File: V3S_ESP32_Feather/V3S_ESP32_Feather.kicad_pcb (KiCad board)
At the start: 4 copper layers, 22.9 x 50.8 mm, 76 parts, among them J1 USB_C_Receptacle_USB2.0, J2 Bat, J4 PWM, J5 U.FL-R-SMT(01), J6 UART, J7 Micro_SD_Card_Det, J8 I2C, J9 SPI, Q1 S8050(SOT-23), U1 V3S, U2 FUSB302B01MPX, U4 ICM-20948, U5 ESP32-PICO-D4, U6 MCP73831T-4ADI_OT, U7 BMP280, U8 INA219AIDCNR, Y1 X1E0000210832, Y2 CC5V-T1A 32.768KHZ +-20PPM 12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

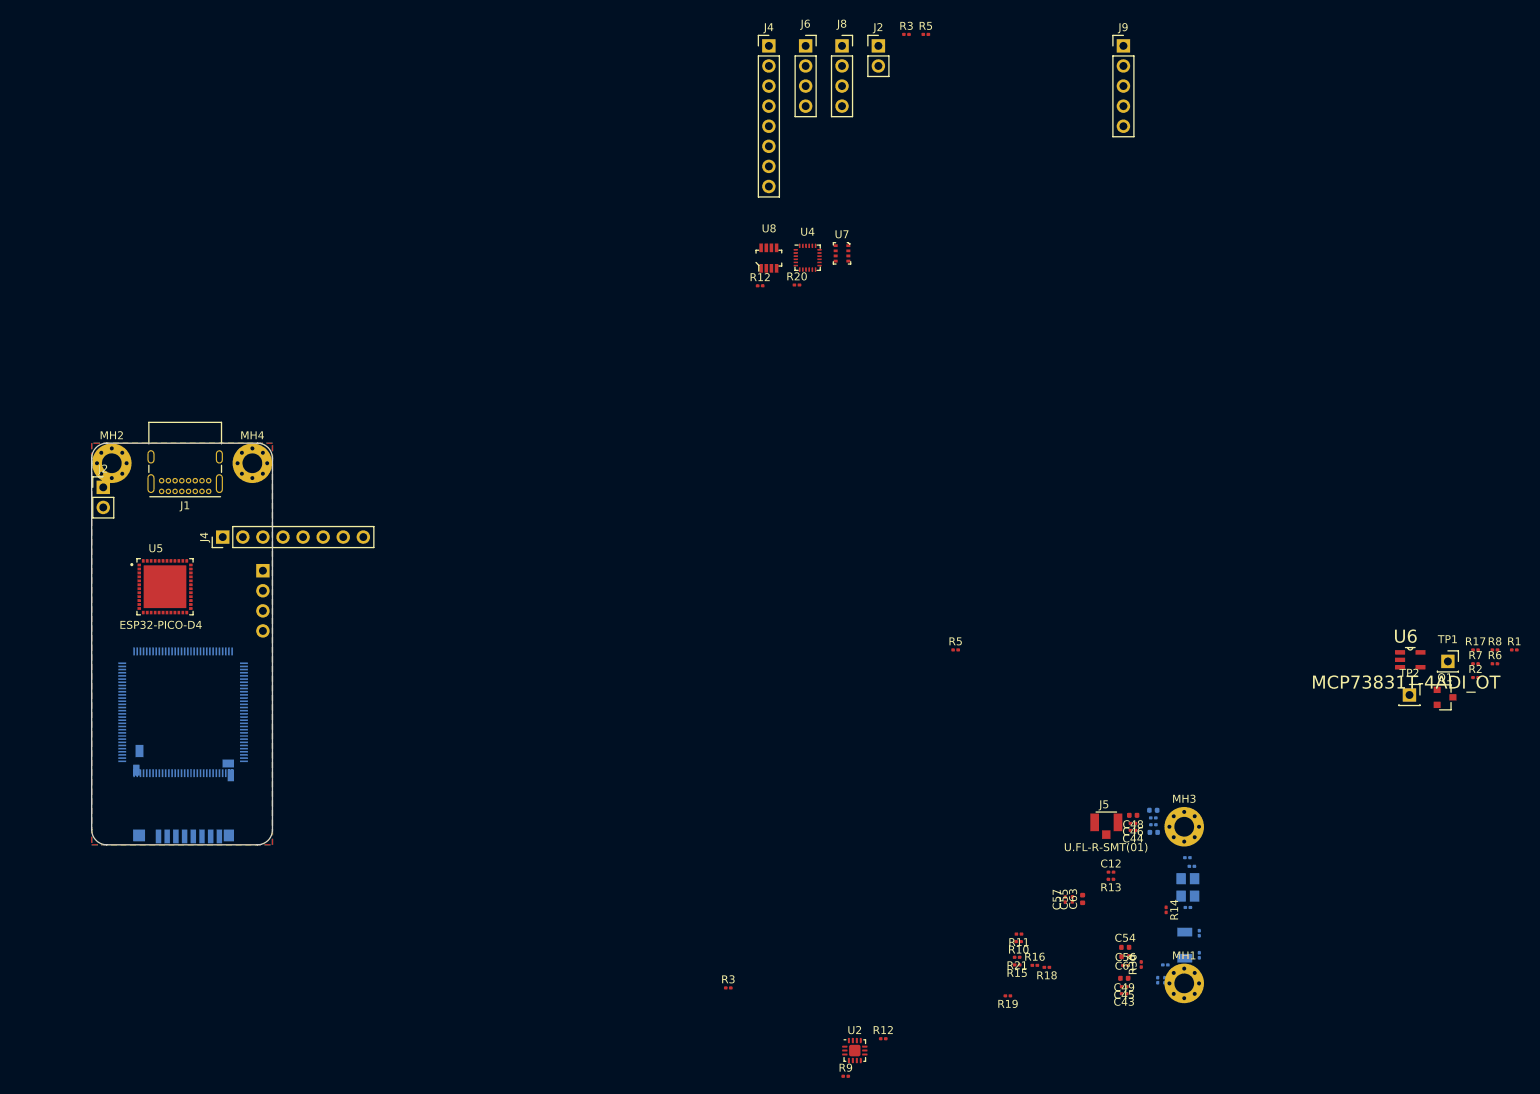
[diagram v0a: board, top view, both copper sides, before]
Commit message: Add more footprint, pcb format done, started component placement
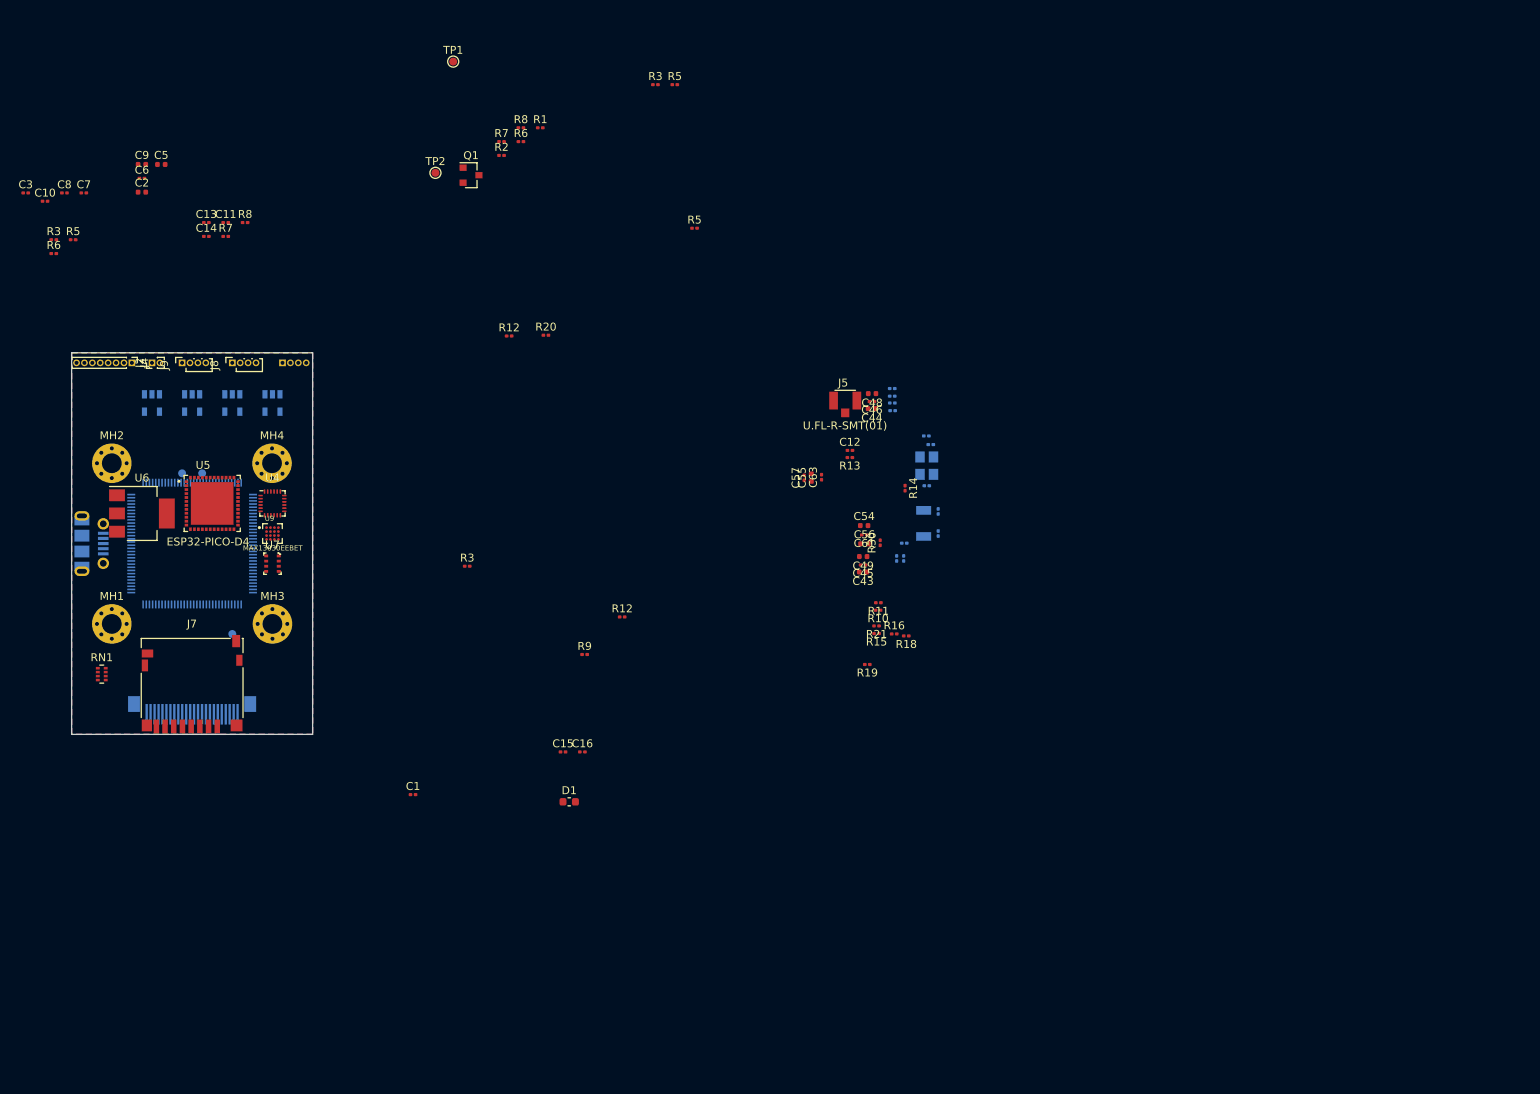
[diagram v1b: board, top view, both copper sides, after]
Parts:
- removed the J2 at (124.9, -18.5)
- removed the J4 at (111.0, -18.5)
- removed the J6 at (115.7, -18.5)
- removed R17: 470R, Resistor_SMD:R_0201_0603Metric
- added C1: 100nF, Capacitor_SMD:C_0201_0603Metric, F.Cu at (66.0, 76.2)
- added C10: 1uF, Capacitor_SMD:C_0201_0603Metric, F.Cu at (19.5, 1.15)
- added C11: 0.1uF, Capacitor_SMD:C_0201_0603Metric, F.Cu at (42.4, 3.85)
- added C13: 1uF, Capacitor_SMD:C_0201_0603Metric, F.Cu at (39.9, 3.85)
- added C14: 0.1uF, Capacitor_SMD:C_0201_0603Metric, F.Cu at (39.9, 5.60)
- added C15: 100nF, Capacitor_SMD:C_0201_0603Metric, F.Cu at (85.0, 70.8)
- added C16: 100nF, Capacitor_SMD:C_0201_0603Metric, F.Cu at (87.5, 70.8)
- added C2: 10uF, Capacitor_SMD:C_0402_1005Metric, F.Cu at (31.8, 0.00)
- added C3: 1uF, Capacitor_SMD:C_0201_0603Metric, F.Cu at (17.1, 0.10)
- added C5: 10uF, Capacitor_SMD:C_0402_1005Metric, F.Cu at (34.2, -3.50)
- added C6: 1uF, Capacitor_SMD:C_0201_0603Metric, F.Cu at (31.8, -1.75)
- added C7: 4.7uF, Capacitor_SMD:C_0201_0603Metric, F.Cu at (24.4, 0.10)
- added C8: 4.7uF, Capacitor_SMD:C_0201_0603Metric, F.Cu at (21.9, 0.10)
- added C9: 10uF, Capacitor_SMD:C_0402_1005Metric, F.Cu at (31.8, -3.50)
- added D1: D, Resistor_SMD:R_0603_1608Metric, F.Cu at (85.8, 77.1)
- added J3: CAM, fpc_cam24:FPC_24_CAM, B.Cu at (38.1, 66.0)
- added R3: 47K, Resistor_SMD:R_0201_0603Metric, F.Cu at (20.6, 6.02)
- added R5: 10K, Resistor_SMD:R_0201_0603Metric, F.Cu at (23.1, 6.02)
- added R6: 10K, Resistor_SMD:R_0201_0603Metric, F.Cu at (20.6, 7.77)
- added R7: R, Resistor_SMD:R_0201_0603Metric, F.Cu at (42.4, 5.60)
- added R8: R, Resistor_SMD:R_0201_0603Metric, F.Cu at (44.8, 3.85)
- added RN1: 47K, Resistor_SMD:R_Array_Concave_4x0402, F.Cu at (26.7, 61.0)
- added TP2: CPU_RX, TestPoint:TestPoint_Pad_D1.0mm, B.Cu at (36.8, 35.6)
- added TP3: CPU_TX, TestPoint:TestPoint_Pad_D1.0mm, B.Cu at (39.4, 35.6)
- added TP4: CPU_RST, TestPoint:TestPoint_Pad_D1.0mm, B.Cu at (43.2, 55.9)
- added U2: MIC5504-1.2YM5, Package_TO_SOT_SMD:SOT-23-5, B.Cu at (43.2, 26.7)
- added U3: MIC5501-3.0YM5, Package_TO_SOT_SMD:SOT-23-5, B.Cu at (33.0, 26.7)
- added U9: MAX13030EEBET, MAX13030EEBET:BGA16C50P4X4_202X202X67N, F.Cu at (48.3, 43.2)
- C43, C44, C55, C56: footprint Capacitor_SMD:C_0201_0603Metric -> Capacitor_SMD:C_0402_1005Metric
- C61, C63, C64, C65: footprint Capacitor_SMD:C_0402_1005Metric -> Capacitor_SMD:C_0201_0603Metric
- J1: value USB_C_Receptacle_USB2.0 -> USB_B_Micro; footprint Connector_USB:USB_C_Receptacle_GCT_USB4085 -> Connector_USB:USB_Micro-B_Molex-105017-0001; moved to B.Cu
- J2: footprint Connector_PinHeader_2.54mm:PinHeader_1x02_P2.54mm_Vertical -> Connector_PinHeader_1.00mm:PinHeader_1x02_P1.00mm_Vertical
- J4: footprint Connector_PinHeader_2.54mm:PinHeader_1x08_P2.54mm_Vertical -> Connector_PinHeader_1.00mm:PinHeader_1x08_P1.00mm_Vertical
- J6: footprint Connector_PinSocket_2.54mm:PinSocket_1x04_P2.54mm_Vertical -> Connector_PinHeader_1.00mm:PinHeader_1x04_P1.00mm_Vertical
- J7: moved to F.Cu
- J8: footprint Connector_PinSocket_2.54mm:PinSocket_1x04_P2.54mm_Vertical -> Connector_PinSocket_1.00mm:PinSocket_1x04_P1.00mm_Vertical
- J9: value SPI -> I2C; footprint Connector_PinHeader_2.54mm:PinHeader_1x05_P2.54mm_Vertical -> Connector_PinSocket_1.00mm:PinSocket_1x04_P1.00mm_Vertical
- R3 (x2): value 5.1K -> 47K
- R5 (x2): value 5.1K -> 10K
- R6: value 100K -> 10K
- R7: value 0 -> R
- R8: value 2K -> R
- TP1: footprint Connector_PinSocket_2.54mm:PinSocket_1x01_P2.54mm_Vertical -> TestPoint:TestPoint_Pad_D1.0mm
- TP2: value CHRG_IN -> CPU_RX; footprint Connector_PinSocket_2.54mm:PinSocket_1x01_P2.54mm_Vertical -> TestPoint:TestPoint_Pad_D1.0mm
- U2: value FUSB302B01MPX -> MIC5504-1.2YM5; footprint Package_DFN_QFN:WQFN-14-1EP_2.5x2.5mm_P0.5mm_EP1.45x1.45mm -> Package_TO_SOT_SMD:SOT-23-5; moved to B.Cu
- U6: value MCP73831T-4ADI_OT -> LT1963AxST-3.3; footprint MCP73831T-4ADI_OT:SOT95P280X145-5N -> Package_TO_SOT_SMD:SOT-223-3_TabPin2
- U8: value INA219AIDCNR -> MIC5504-1.8YM5; footprint digikey-footprints:SOT-23-8 -> Package_TO_SOT_SMD:SOT-23-5; moved to B.Cu
- moved U6 161.5 mm to (31.8, 40.6)
- moved TP1 146.9 mm to (71.1, -16.5)
- moved MH1 143.1 mm to (27.9, 54.6)
- moved R1 139.8 mm to (82.1, -8.14)
- moved Q1 139.8 mm to (73.4, -2.14)
- moved R2 139.8 mm to (77.2, -4.64)
- moved R6 139.8 mm to (79.7, -6.39)
- moved R7 139.8 mm to (77.2, -6.39)
- moved R8 139.8 mm to (79.7, -8.14)
- moved TP2 139.8 mm to (68.9, -2.44)
- moved J9 125.6 mm to (36.8, 21.6), turned to 90 degrees
- moved MH3 118.1 mm to (48.3, 54.6)
- moved U2 110.1 mm to (48.3, 26.7), turned to 270 degrees
- moved J8 86.9 mm to (43.2, 21.6), turned to 90 degrees
- moved U7 82.0 mm to (48.3, 47.0)
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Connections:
- C44 pad 1: +3.3VA -> +3V3
- C46 pad 1: +3.3VA -> +3V3
- C48 pad 1: +3.3VA -> +3V3
- C54 pad 1: +3.3VA -> +3V3
- C56 pad 1: +3.3VA -> +3V3
- C61 pad 2: +3.3VA -> +3V3
- J6 pad 3: /TX -> (no net)
- J7 pad 10: Net-(J7-Pad10) -> (no net)
- J7 pad 9: Net-(J7-Pad9) -> (no net)
- J9 pad 2: /All V3s input output/SPI_MISO -> Net-(J9-Pad2)
- J9 pad 3: /All V3s input output/SPI_CLK -> Net-(J9-Pad3)
- J9 pad 4: /All V3s input output/SPI_MOSI -> +3V3
- Q1 pad 2: Net-(C2-Pad1) -> /PMIC Power Battery/VIN
- R3 pad 1: GND -> +3V3 (x2)
- R3 pad 2: Net-(J1-PadA5) -> /USB_ID (x2)
- R5 pad 1: GND -> +3V3 (x2)
- R5 pad 2: Net-(J1-PadB5) -> Net-(J9-Pad2) (x2)
- R6 pad 1: /PMIC Power Battery/3.3V_EN -> Net-(J9-Pad3)
- R6 pad 2: Net-(C2-Pad1) -> +3V3
- R7 pad 1: Net-(R7-Pad1) -> +BATT
- R7 pad 2: VBUS -> GND
- R8 pad 2: GND -> +BATT
- TP2 pad 1: Net-(R7-Pad1) -> /UART_RX_D0
- U1 pad 10: Net-(U1-Pad10) -> (no net)
- U1 pad 100: /All V3s input output/USB_INT -> /USB_ID
- U1 pad 104: +3.3VA -> +3V3
- U1 pad 109: +3.3VA -> +3V3
- U1 pad 11: Net-(U1-Pad11) -> (no net)
- U1 pad 112: Net-(U1-Pad112) -> (no net)
- U1 pad 113: Net-(U1-Pad113) -> (no net)
- U1 pad 114: Net-(U1-Pad114) -> (no net)
- U1 pad 115: +3.3VA -> +3V0
- U1 pad 119: /All V3s input output/HBIAS -> GND
- U1 pad 120: Net-(U1-Pad120) -> (no net)
- U1 pad 121: Net-(U1-Pad121) -> (no net)
- U1 pad 124: Net-(U1-Pad124) -> (no net)
- U1 pad 125: Net-(U1-Pad125) -> (no net)
- U1 pad 127: +3.3VA -> +3V3
- U1 pad 13: Net-(U1-Pad13) -> (no net)
- U1 pad 14: Net-(U1-Pad14) -> (no net)
- U1 pad 43: Net-(U1-Pad43) -> (no net)
- U1 pad 44: Net-(U1-Pad44) -> (no net)
- U1 pad 45: /All V3s input output/I2C0_CLK -> Net-(J9-Pad2)
- U1 pad 46: /All V3s input output/I2C0_SDA -> Net-(J9-Pad3)
- U1 pad 50: +3.3VA -> +3V3
- U1 pad 52: /All V3s input output/SPI_MISO -> (no net)
- U1 pad 53: /All V3s input output/SPI_CLK -> (no net)
- U1 pad 54: Net-(U1-Pad54) -> (no net)
- U1 pad 55: /All V3s input output/SPI_MOSI -> (no net)
- U1 pad 57: +3.3VA -> +3V3
- U1 pad 6: Net-(U1-Pad6) -> (no net)
- U1 pad 7: Net-(U1-Pad7) -> (no net)
- U1 pad 76: +3.3VA -> +3V0
- U1 pad 77: Net-(U1-Pad77) -> (no net)
- U1 pad 78: Net-(U1-Pad78) -> (no net)
- U1 pad 81: Net-(U1-Pad81) -> (no net)
- U1 pad 82: Net-(U1-Pad82) -> (no net)
- U1 pad 83: Net-(U1-Pad83) -> (no net)
- U1 pad 84: Net-(U1-Pad84) -> (no net)
- U1 pad 86: Net-(U1-Pad86) -> (no net)
- U1 pad 87: Net-(U1-Pad87) -> (no net)
- U1 pad 89: Net-(U1-Pad89) -> (no net)
- U1 pad 90: Net-(U1-Pad90) -> (no net)
- U1 pad 91: Net-(U1-Pad91) -> (no net)
- U1 pad 92: Net-(U1-Pad92) -> (no net)
- U1 pad 93: +3.3VA -> +3V3
- U1 pad 98: /PMIC Power Battery/VCC_RTC -> +3V0
- U2 pad 1: /All V3s input output/CC2 -> /PMIC Power Battery/VIN
- U2 pad 2: /All V3s input output/VBUS -> GND
- U2 pad 3: +3V3 -> /PMIC Power Battery/VIN
- U2 pad 4: +3V3 -> Net-(U2-Pad4)
- U2 pad 5: /All V3s input output/USB_INT -> +1V2
- U4 pad 1: Net-(U4-Pad1) -> (no net)
- U4 pad 11: Net-(U4-Pad11) -> GND
- U4 pad 12: Net-(U4-Pad12) -> /WIFI, BT, RT/ICM_INT1.8
- U4 pad 13: Net-(U4-Pad13) -> +1V8
- U4 pad 14: Net-(U4-Pad14) -> (no net)
- U4 pad 15: Net-(U4-Pad15) -> (no net)
- U4 pad 16: Net-(U4-Pad16) -> (no net)
- U4 pad 17: Net-(U4-Pad17) -> (no net)
- U4 pad 18: Net-(U4-Pad18) -> GND
- U4 pad 19: Net-(U4-Pad19) -> (no net)
- U4 pad 2: Net-(U4-Pad2) -> (no net)
- U4 pad 20: Net-(U4-Pad18) -> GND
- U4 pad 21: Net-(U4-Pad21) -> (no net)
- U4 pad 22: Net-(U4-Pad22) -> /WIFI, BT, RT/CS1.8
- U4 pad 23: Net-(U4-Pad23) -> /WIFI, BT, RT/CLK1.8
- U4 pad 24: Net-(U4-Pad24) -> /WIFI, BT, RT/MOSI1.8
- U4 pad 3: Net-(U4-Pad3) -> (no net)
- U4 pad 4: Net-(U4-Pad4) -> (no net)
- U4 pad 5: Net-(U4-Pad5) -> (no net)
- U4 pad 6: Net-(U4-Pad6) -> (no net)
- U4 pad 7: Net-(U4-Pad7) -> (no net)
- U4 pad 8: Net-(U4-Pad8) -> +1V8
- U4 pad 9: Net-(U4-Pad9) -> /WIFI, BT, RT/MISO1.8
- U5 pad 11: /WIFI, BT, RT/IO35 -> (no net)
- U5 pad 25: Net-(U5-Pad25) -> (no net)
- U5 pad 26: Net-(U5-Pad26) -> (no net)
- U5 pad 27: Net-(U5-Pad27) -> (no net)
- U5 pad 28: Net-(U5-Pad28) -> (no net)
- U5 pad 29: Net-(U5-Pad29) -> (no net)
- U5 pad 30: Net-(U5-Pad30) -> (no net)
- U5 pad 31: Net-(U5-Pad31) -> (no net)
- U5 pad 32: Net-(U5-Pad32) -> (no net)
- U5 pad 33: Net-(U5-Pad33) -> (no net)
- U5 pad 5: Net-(U5-Pad5) -> (no net)
- U5 pad 6: Net-(U5-Pad6) -> /WIFI, BT, RT/ICM_INT
- U5 pad 7: Net-(U5-Pad7) -> Net-(R8-Pad1)
- U6 pad 1: Net-(R17-Pad2) -> /PMIC Power Battery/VIN
- U6 pad 3: +BATT -> +3V3
- U7 pad 1: Net-(U7-Pad1) -> GND
- U7 pad 2: Net-(U7-Pad2) -> +3V3
- U7 pad 3: Net-(U7-Pad3) -> /SDA
- U7 pad 4: Net-(U7-Pad4) -> /SCL
- U7 pad 5: Net-(U7-Pad5) -> GND
- U7 pad 6: Net-(U7-Pad6) -> +3V3
- U7 pad 7: Net-(U7-Pad7) -> GND
- U7 pad 8: Net-(U7-Pad8) -> +3V3
- U8 pad 1: Net-(U8-Pad1) -> /PMIC Power Battery/VIN
- U8 pad 2: Net-(U8-Pad2) -> GND
- U8 pad 3: Net-(U8-Pad3) -> /PMIC Power Battery/VIN
- U8 pad 4: Net-(U8-Pad4) -> (no net)
- U8 pad 5: Net-(U8-Pad5) -> +1V8
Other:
- board size 22.9 x 50.8 mm -> 30.5 x 48.3 mm

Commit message: New component placement, progress on rooting
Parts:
- removed C2: 10uF, Capacitor_SMD:C_0402_1005Metric
- removed Q1: S8050(SOT-23), Package_TO_SOT_SMD:SOT-23
- removed R2: 100K, Resistor_SMD:R_0201_0603Metric
- removed TP1: PWR_SRC, TestPoint:TestPoint_Pad_D1.0mm
- removed the TP2 at (68.9, -2.44)
- removed the U2 at (48.3, 26.7)
- C10, C3, C43, C44, C45, C46, C48, C49, C55, C57, C6, C63, R10, R11, R30, U6: moved to B.Cu
- J2: footprint Connector_PinHeader_1.00mm:PinHeader_1x02_P1.00mm_Vertical -> Connector_JST:JST_SH_SM02B-SRSS-TB_1x02-1MP_P1.00mm_Horizontal
- J4: footprint Connector_PinHeader_1.00mm:PinHeader_1x08_P1.00mm_Vertical -> Connector_JST:JST_SH_SM08B-SRSS-TB_1x08-1MP_P1.00mm_Horizontal
- J6: footprint Connector_PinHeader_1.00mm:PinHeader_1x04_P1.00mm_Vertical -> Connector_JST:JST_SH_SM04B-SRSS-TB_1x04-1MP_P1.00mm_Horizontal; moved to F.Cu
- J8, J9: footprint Connector_PinSocket_1.00mm:PinSocket_1x04_P1.00mm_Vertical -> Connector_JST:JST_SH_SM04B-SRSS-TB_1x04-1MP_P1.00mm_Horizontal
- moved C48 100.0 mm to (24.2, 30.6), turned to 0 degrees
- moved C44 100.0 mm to (24.3, 33.0), turned to 0 degrees
- moved C46 100.0 mm to (24.3, 31.8), turned to 0 degrees
- moved C37 99.6 mm to (31.9, 32.3), turned to 270 degrees
- moved R4 99.0 mm to (32.0, 34.0), turned to 90 degrees
- moved Y1 96.4 mm to (34.6, 32.8), turned to 0 degrees
- moved C36 94.0 mm to (37.1, 32.8), turned to 90 degrees
- moved C41 91.8 mm to (41.1, 30.9), turned to 180 degrees
- moved C40 89.4 mm to (43.9, 30.9), turned to 0 degrees
- moved Y2 88.4 mm to (42.7, 32.7), turned to 270 degrees
- moved C49 86.8 mm to (38.4, 26.7), turned to 0 degrees
- moved C45 86.8 mm to (38.4, 27.9), turned to 0 degrees
- moved C43 86.7 mm to (38.4, 29.2), turned to 0 degrees
- moved R30 86.2 mm to (39.6, 33.3), turned to 270 degrees
- moved R13 84.9 mm to (36.6, 38.9), turned to 90 degrees
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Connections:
- C5 pad 1: /PMIC Power Battery/VIN -> +BATT
- D1 pad 1: /PMIC Power Battery/VIN -> +BATT
- J3 pad 1: (no net) -> /All V3s input output/STROBE
- J3 pad 10: (no net) -> Net-(J3-Pad10)
- J4 pad 1: GND -> /IO34
- J4 pad 2: /IO34 -> /IO35
- J4 pad 3: /IO33 -> /IO32
- J4 pad 4: /IO32 -> /IO33
- J4 pad 5: /IO27 -> /IO25
- J4 pad 7: /IO25 -> /IO27
- J6 pad 3: (no net) -> /TX
- J7 pad 10: (no net) -> Net-(J7-Pad10)
- J7 pad 9: (no net) -> Net-(J7-Pad9)
- R1 pad 1: VBUS -> Net-(D1-Pad2)
- R1 pad 2: Net-(D1-Pad2) -> VBUS
- RN1 pad 1: /All V3s input output/PF4 -> /All V3s input output/PF0
- RN1 pad 2: /All V3s input output/PF3 -> /All V3s input output/PF1
- RN1 pad 3: /All V3s input output/PF1 -> /All V3s input output/PF3
- RN1 pad 4: /All V3s input output/PF0 -> /All V3s input output/PF4
- U1 pad 10: (no net) -> Net-(U1-Pad10)
- U1 pad 11: (no net) -> Net-(U1-Pad11)
- U1 pad 112: (no net) -> Net-(U1-Pad112)
- U1 pad 113: (no net) -> Net-(U1-Pad113)
- U1 pad 114: (no net) -> Net-(U1-Pad114)
- U1 pad 120: (no net) -> Net-(U1-Pad120)
- U1 pad 121: (no net) -> Net-(U1-Pad121)
- U1 pad 124: (no net) -> Net-(U1-Pad124)
- U1 pad 125: (no net) -> Net-(U1-Pad125)
- U1 pad 13: (no net) -> Net-(U1-Pad13)
- U1 pad 14: (no net) -> Net-(U1-Pad14)
- U1 pad 43: (no net) -> Net-(U1-Pad43)
- U1 pad 44: (no net) -> Net-(U1-Pad44)
- U1 pad 52: (no net) -> Net-(U1-Pad52)
- U1 pad 53: (no net) -> Net-(U1-Pad53)
- U1 pad 54: (no net) -> Net-(U1-Pad54)
- U1 pad 55: (no net) -> Net-(U1-Pad55)
- U1 pad 6: (no net) -> Net-(U1-Pad6)
- U1 pad 7: (no net) -> Net-(U1-Pad7)
- U1 pad 77: (no net) -> Net-(U1-Pad77)
- U1 pad 78: (no net) -> Net-(U1-Pad78)
- U1 pad 81: (no net) -> Net-(U1-Pad81)
- U1 pad 82: (no net) -> Net-(U1-Pad82)
- U1 pad 83: (no net) -> Net-(U1-Pad83)
- U1 pad 84: (no net) -> Net-(U1-Pad84)
- U1 pad 86: (no net) -> Net-(U1-Pad86)
- U1 pad 87: (no net) -> Net-(U1-Pad87)
- U1 pad 89: (no net) -> Net-(U1-Pad89)
- U1 pad 90: (no net) -> Net-(U1-Pad90)
- U1 pad 91: (no net) -> Net-(U1-Pad91)
- U1 pad 92: (no net) -> Net-(U1-Pad92)
- U2 pad 1: /PMIC Power Battery/VIN -> +BATT
- U2 pad 3: /PMIC Power Battery/VIN -> +BATT
- U3 pad 1: /PMIC Power Battery/VIN -> +BATT
- U3 pad 3: /PMIC Power Battery/VIN -> +BATT
- U3 pad 4: (no net) -> Net-(U3-Pad4)
- U4 pad 1: (no net) -> Net-(U4-Pad1)
- U4 pad 14: (no net) -> Net-(U4-Pad14)
- U4 pad 15: (no net) -> Net-(U4-Pad15)
- U4 pad 16: (no net) -> Net-(U4-Pad16)
- U4 pad 17: (no net) -> Net-(U4-Pad17)
- U4 pad 19: (no net) -> Net-(U4-Pad19)
- U4 pad 2: (no net) -> Net-(U4-Pad2)
- U4 pad 21: (no net) -> Net-(U4-Pad21)
- U4 pad 3: (no net) -> Net-(U4-Pad3)
- U4 pad 4: (no net) -> Net-(U4-Pad4)
- U4 pad 5: (no net) -> Net-(U4-Pad5)
- U4 pad 6: (no net) -> Net-(U4-Pad6)
- U4 pad 7: (no net) -> Net-(U4-Pad7)
- U5 pad 11: (no net) -> /IO35
- U5 pad 25: (no net) -> Net-(U5-Pad25)
- U5 pad 26: (no net) -> Net-(U5-Pad26)
- U5 pad 27: (no net) -> Net-(U5-Pad27)
- U5 pad 28: (no net) -> /TX
- U5 pad 29: (no net) -> /WIFI, BT, RT/SD3
- U5 pad 30: (no net) -> Net-(U5-Pad30)
- U5 pad 31: (no net) -> Net-(U5-Pad31)
- U5 pad 32: (no net) -> Net-(U5-Pad32)
- U5 pad 33: (no net) -> Net-(U5-Pad33)
- U5 pad 5: (no net) -> Net-(U5-Pad5)
- U6 pad 1: /PMIC Power Battery/VIN -> +BATT
- U8 pad 1: /PMIC Power Battery/VIN -> +BATT
- U8 pad 3: /PMIC Power Battery/VIN -> +BATT
- U8 pad 4: (no net) -> Net-(U8-Pad4)
- U9 pad A1: (no net) -> Net-(U9-PadA1)
- U9 pad A2: (no net) -> Net-(U9-PadA2)
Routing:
- net +BATT: track 0.00 -> 30.2 mm
- net /SDA: track 0.00 -> 26.8 mm
- net /SCL: track 0.00 -> 24.3 mm
- net /All V3s input output/~CSI_RST: track 0.00 -> 24.1 mm, vias 0 -> 2
- net /All V3s input output/SDIO1_CLK: track 0.00 -> 21.2 mm, vias 0 -> 1
- net /IO27: track 0.00 -> 19.6 mm
- net /IO26: track 0.00 -> 18.8 mm
- net /All V3s input output/SDIO1_CMD: track 0.00 -> 18.1 mm, vias 0 -> 1
- net /IO25: track 0.00 -> 18.0 mm
- net /All V3s input output/SDIO1_DAT2: track 0.00 -> 17.7 mm, vias 0 -> 1
- net /IO33: track 0.00 -> 17.3 mm
- net /IO34: track 0.00 -> 17.1 mm
- net /IO35: track 0.00 -> 16.9 mm
- net /IO32: track 0.00 -> 16.7 mm
- net /All V3s input output/SDIO1_DAT0: track 0.00 -> 16.2 mm, vias 0 -> 1
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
